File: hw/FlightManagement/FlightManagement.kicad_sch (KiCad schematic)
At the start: 74 parts, among them J2 B4B-EH-A(LF)(SN), J3 B6B-EH-A(LF)(SN), J4 Micro_SD_Card, J6 Conn_01x02_Socket, J7 Conn_01x02_Pin, U1 YTS1C0033BBG01, U12 TPS54202DDC, U14 SN74LVC1G125DBV, U15 SN74LVC1G125DBV, U2 STM32L431RCTx, U3 MPU-6050, U4 LIS2MDL, U8 SN65HVD230, U9 W25Q128JVS, Y4 Crystal_GND24

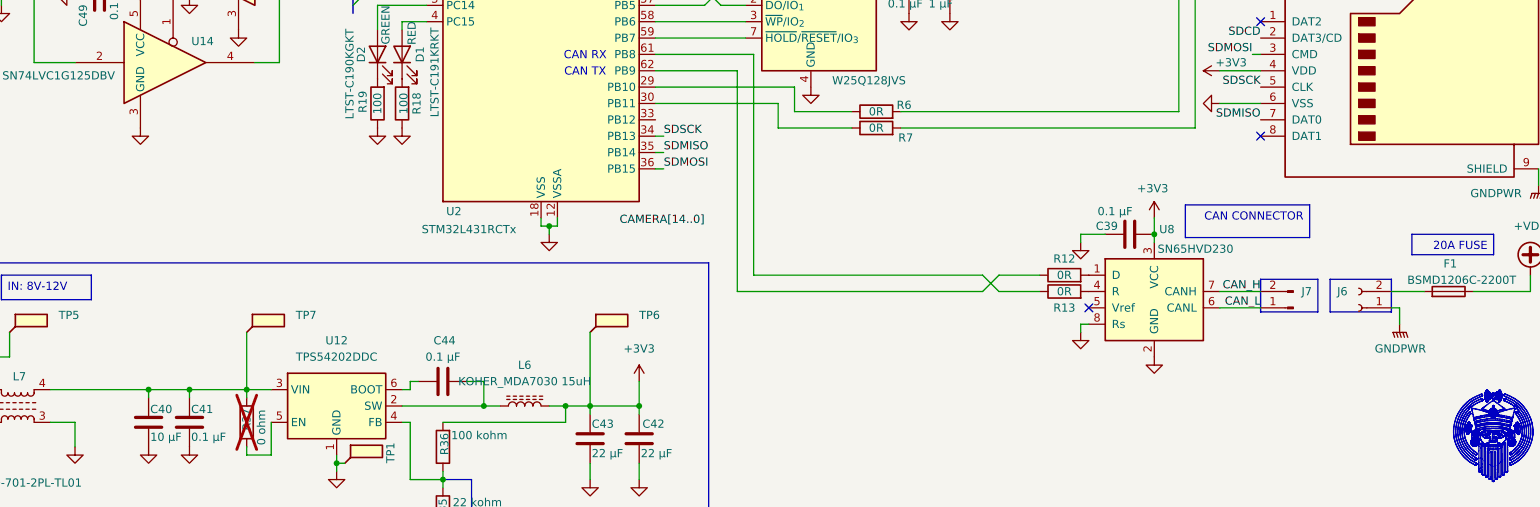
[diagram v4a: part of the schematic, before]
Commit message: finish fmu routing
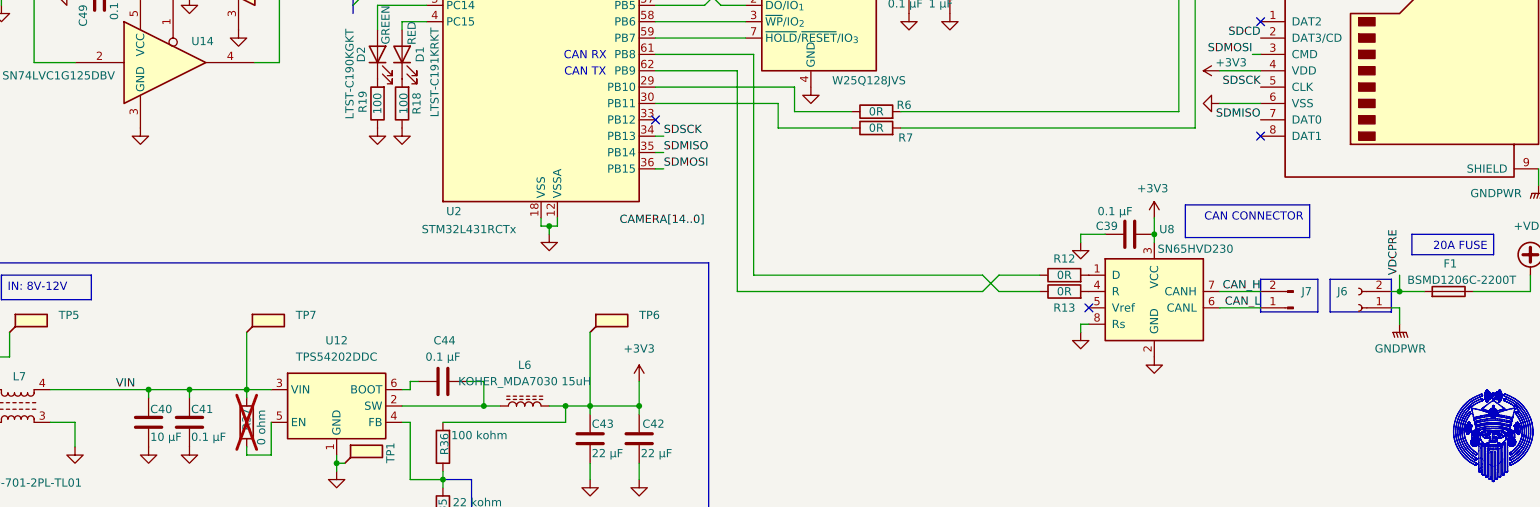
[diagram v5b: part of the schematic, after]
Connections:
- net VDCPRE: now reaches F1.2, J6.2 (Pin_2)
- net VIN: now reaches C40.1, C41.1, L7.4, R37.1, TP7.1, U12.3 (VIN)
- no-connect marks 4 -> 5
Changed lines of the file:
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@@
 	)
 	(junction
+		(at 261.62 151.13)
+		(diameter 0)
+		(color 0 0 0 0)
+	)
+	(junction
 		(at 194.31 53.34)
 		(diameter 0)
@@
 	)
 	(no_connect
+		(at 146.05 124.46)
+	)
+	(no_connect
 		(at 240.03 109.22)
 	)
@@
 	(wire
 		(pts
-			(xy 260.35 151.13) (xy 265.43 151.13)
+			(xy 260.35 151.13) (xy 261.62 151.13)
 		)
 		(stroke
@@
 	(wire
 		(pts
+			(xy 261.62 151.13) (xy 265.43 151.13)
+		)
+		(stroke
+			(width 0)
+			(type default)
+		)
+	)
+	(wire
+		(pts
 			(xy 127 24.13) (xy 127 25.4)
 		)
@@
 	(wire
 		(pts
+			(xy 261.62 148.59) (xy 261.62 151.13)
+		)
+		(stroke
+			(width 0)
+			(type default)
+		)
+	)
+	(wire
+		(pts
 			(xy 189.23 53.34) (xy 189.23 55.88)
 		)
@@
 		)
 	)
+	(label "VIN"
+		(at 62.23 166.37 0)
+		(effects
+			(font
+				(size 1.27 1.27)
+			)
+			(justify left bottom)
+		)
+	)
 	(label "CAMERA[14..0]"
 		(at 241.3 48.26 0)
@@
 		)
 	)
+	(label "VDCPRE"
+		(at 261.62 148.59 90)
+		(effects
+			(font
+				(size 1.27 1.27)
+			)
+			(justify left bottom)
+		)
+	)

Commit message: FMU completed
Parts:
- renumbered C40 to C1, C8 to C10, C10 to C11, C7 to C12, C9 to C13, C12 to C15, C15 to C16, C14 to C17, C13 to C18, C2 to C19, C41 to C2, C3 to C20, C5 to C22, C4 to C24, C6 to C25, C44 to C3, C43 to C4, C39 to C42, C45 to C43, C51 to C44, C52 to C45, C50 to C46, C48 to C47, C46 to C48, C42 to C5, C1 to C50, C11 to C6, C16 to C8, D11 to D1, D1 to D3, J7 to J1, J6 to J2, J2 to J5, J4 to J6, L7 to L1, L6 to L2, R36 to R1, R18 to R11, R2 to R12, R19 to R13, R3 to R15, R13 to R19, R35 to R2, R12 to R20, R6 to R21, R1 to R22, R37 to R3, R9 to R5, R5 to R6, R24 to R8, R8 to R9, TP5 to TP1, TP7 to TP2, TP6 to TP3, TP1 to TP4, U12 to U1, U15 to U10, U9 to U11, U14 to U12, U4 to U2, U2 to U4, U1 to U7, U8 to U9, Y4 to Y1

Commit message: start working on firmware
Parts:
- D2: renamed from D3; PN LTST-C191KRKT -> NCD0603R1
- D3: renamed from D2; PN LTST-C190KGKT -> NCD0603C1
- L1: PNALT (none) -> PCAQ7060MW-701
- renumbered C17 to C11, C8 to C12, C6 to C14, C16 to C15, C15 to C16, C18 to C17, C25 to C19, C24 to C20, C20 to C24, C19 to C25, C47 to C43, C43 to C44, C44 to C45, C45 to C47, C50 to C51, C49 to C52, C13 to C6, C12 to C8, C11 to C9, R3 to R1, R15 to R10, R13 to R14, R11 to R15, R1 to R3, R9 to R8, R8 to R9, TP2 to TP1, TP1 to TP2, U3 to U2, U2 to U3
